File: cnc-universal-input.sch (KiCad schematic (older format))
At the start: 161 parts, among them J1 SA, J10 pwr-in, J11 output, J12 USB_B_Mini, J13 ext-pwr, J2 SB, J3 SC, J4 SD, J5 SE, J6 SF, J7 SG, J8 SH, J9 AVR-ISP-6, Q1 2N7002, Q10 IRLML2244TRPBF, Q11 2N7002, Q12 2N7002, Q13 2N7002, Q2 2N7002, Q3 2N7002, Q4 2N7002, Q5 2N7002, Q6 2N7002, Q7 2N7002, Q8 2N7002, Q9 2N7002, SW1 RESET, SW2 BTN, U1 ATmega328PB, U10 SFH617A-4, U11 SFH617A-4, U12 SFH617A-4, U13 SFH617A-4, U14 SFH617A-4, U15 SFH617A-4, U16 SFH617A-4, U17 SFH617A-4, U18 CH340G, U2 74HC595, U3 74HC595, U4 74HC595, U5 4051, U6 L7812, U7 L7805, U8 LM7321, U9 SFH617A-4, Y1 20Mhz, Y2 12MHz

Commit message: Fixed 340G isolation issue
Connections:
- net labels removed: VBUS
- wire segments 586 -> 580
- no-connect marks 12 -> 13
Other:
- moved on the sheet: C10, C21
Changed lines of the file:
@@
 Wire Wire Line
 	14600 6050 14600 6100
-$Comp
-L power:VBUS #PWR0175
-U 1 1 600B49CF
-P 14600 4500
-F 0 "#PWR0175" H 14600 4350 50  0001 C CNN
-F 1 "VBUS" H 14615 4673 50  0000 C CNN
-F 2 "" H 14600 4500 50  0001 C CNN
-F 3 "" H 14600 4500 50  0001 C CNN
-	1    14600 4500
-	1    0    0    -1
-$EndComp
 Wire Wire Line
 	14600 4500 14600 4850
@@
 	15400 4550 15400 4500
 $Comp
-L power:VBUS #PWR0177
-U 1 1 609D5862
-P 15150 4500
-F 0 "#PWR0177" H 15150 4350 50  0001 C CNN
-F 1 "VBUS" H 15165 4673 50  0000 C CNN
-F 2 "" H 15150 4500 50  0001 C CNN
-F 3 "" H 15150 4500 50  0001 C CNN
-	1    15150 4500
-	1    0    0    -1
-$EndComp
-$Comp
-L power:VBUS #PWR0178
-U 1 1 609D5BF4
-P 15400 4500
-F 0 "#PWR0178" H 15400 4350 50  0001 C CNN
-F 1 "VBUS" H 15415 4673 50  0000 C CNN
-F 2 "" H 15400 4500 50  0001 C CNN
-F 3 "" H 15400 4500 50  0001 C CNN
-	1    15400 4500
-	1    0    0    -1
-$EndComp
-$Comp
 L cnc-universal-input-rescue:USB_B_Mini-Connector J12
 U 1 1 609D7711
@@
 NoConn ~ 13450 5550
 $Comp
-L power:VBUS #PWR0179
-U 1 1 60ABEF15
-P 13500 4500
-F 0 "#PWR0179" H 13500 4350 50  0001 C CNN
-F 1 "VBUS" H 13515 4673 50  0000 C CNN
-F 2 "" H 13500 4500 50  0001 C CNN
-F 3 "" H 13500 4500 50  0001 C CNN
-	1    13500 4500
-	1    0    0    -1
-$EndComp
-Wire Wire Line
-	13500 4500 13500 4750
-Wire Wire Line
-	13500 5150 13450 5150
-$Comp
 L power:GND #PWR0180
 U 1 1 60B0DB32
@@
 L Device:CP_Small C10
 U 1 1 6112AB08
-P 13750 4900
-F 0 "C10" V 13838 4946 50  0000 L CNN
-F 1 "10uF" V 13600 4750 50  0000 L CNN
-F 2 "Capacitor_Tantalum_SMD:CP_EIA-6032-28_Kemet-C" H 13750 4900 50  0001 C CNN
-F 3 "~" H 13750 4900 50  0001 C CNN
-	1    13750 4900
-	1    0    0    -1
-$EndComp
-Wire Wire Line
-	13750 4800 13750 4750
-Wire Wire Line
-	13750 4750 13500 4750
-Connection ~ 13500 4750
-Wire Wire Line
-	13500 4750 13500 5150
+P 15300 5950
+F 0 "C10" V 15388 5996 50  0000 L CNN
+F 1 "10uF" V 15150 5800 50  0000 L CNN
+F 2 "Capacitor_Tantalum_SMD:CP_EIA-6032-28_Kemet-C" H 15300 5950 50  0001 C CNN
+F 3 "~" H 15300 5950 50  0001 C CNN
+	1    15300 5950
+	1    0    0    -1
+$EndComp
 $Comp
 L power:GND #PWR0181
 U 1 1 6117C62D
-P 13750 5050
-F 0 "#PWR0181" H 13750 4800 50  0001 C CNN
-F 1 "GND" H 13755 4877 50  0000 C CNN
-F 2 "" H 13750 5050 50  0001 C CNN
-F 3 "" H 13750 5050 50  0001 C CNN
-	1    13750 5050
-	1    0    0    -1
-$EndComp
-Wire Wire Line
-	13750 5000 13750 5050
+P 15300 6050
+F 0 "#PWR0181" H 15300 5800 50  0001 C CNN
+F 1 "GND" H 15305 5877 50  0000 C CNN
+F 2 "" H 15300 6050 50  0001 C CNN
+F 3 "" H 15300 6050 50  0001 C CNN
+	1    15300 6050
+	1    0    0    -1
+$EndComp
 Wire Notes Line
 	15800 4200 15800 6400
@@
 L Device:C_Small C21
 U 1 1 605F6BC3
-P 15350 6000
-F 0 "C21" H 15442 6046 50  0000 L CNN
-F 1 "100nF" V 15550 5750 50  0000 L CNN
-F 2 "Capacitor_SMD:C_0805_2012Metric" H 15350 6000 50  0001 C CNN
-F 3 "~" H 15350 6000 50  0001 C CNN
-	1    15350 6000
+P 15550 5950
+F 0 "C21" H 15642 5996 50  0000 L CNN
+F 1 "100nF" V 15750 5700 50  0000 L CNN
+F 2 "Capacitor_SMD:C_0805_2012Metric" H 15550 5950 50  0001 C CNN
+F 3 "~" H 15550 5950 50  0001 C CNN
+	1    15550 5950
 	1    0    0    -1
 $EndComp
@@
 L power:GND #PWR0198
 U 1 1 605F6BCF
-P 15350 6100
-F 0 "#PWR0198" H 15350 5850 50  0001 C CNN
-F 1 "GND" H 15350 5950 50  0000 C CNN
-F 2 "" H 15350 6100 50  0001 C CNN
-F 3 "" H 15350 6100 50  0001 C CNN
-	1    15350 6100
-	1    0    0    -1
-$EndComp
-$Comp
-L power:VBUS #PWR0199
-U 1 1 6064EB08
-P 15350 5900
-F 0 "#PWR0199" H 15350 5750 50  0001 C CNN
-F 1 "VBUS" H 15365 6073 50  0000 C CNN
-F 2 "" H 15350 5900 50  0001 C CNN
-F 3 "" H 15350 5900 50  0001 C CNN
-	1    15350 5900
+P 15550 6050
+F 0 "#PWR0198" H 15550 5800 50  0001 C CNN
+F 1 "GND" H 15550 5900 50  0000 C CNN
+F 2 "" H 15550 6050 50  0001 C CNN
+F 3 "" H 15550 6050 50  0001 C CNN
+	1    15550 6050
 	1    0    0    -1
 $EndComp
@@
 	1    0    0    -1
 $EndComp
+NoConn ~ 13450 5150
+$Comp
+L power:+5V #PWR0175
+U 1 1 6034F777
+P 14600 4500
+F 0 "#PWR0175" H 14600 4350 50  0001 C CNN
+F 1 "+5V" H 14615 4673 50  0000 C CNN
+F 2 "" H 14600 4500 50  0001 C CNN
+F 3 "" H 14600 4500 50  0001 C CNN
+	1    14600 4500
+	1    0    0    -1
+$EndComp
+$Comp
+L power:+5V #PWR0177
+U 1 1 60350634
+P 15150 4500
+F 0 "#PWR0177" H 15150 4350 50  0001 C CNN
+F 1 "+5V" H 15165 4673 50  0000 C CNN
+F 2 "" H 15150 4500 50  0001 C CNN
+F 3 "" H 15150 4500 50  0001 C CNN
+	1    15150 4500
+	1    0    0    -1
+$EndComp
+$Comp
+L power:+5V #PWR0179
+U 1 1 60469C21
+P 15550 5850
+F 0 "#PWR0179" H 15550 5700 50  0001 C CNN
+F 1 "+5V" H 15565 6023 50  0000 C CNN
+F 2 "" H 15550 5850 50  0001 C CNN
+F 3 "" H 15550 5850 50  0001 C CNN
+	1    15550 5850
+	1    0    0    -1
+$EndComp
+$Comp
+L power:+5V #PWR0199
+U 1 1 604C7554
+P 15300 5850
+F 0 "#PWR0199" H 15300 5700 50  0001 C CNN
+F 1 "+5V" H 15315 6023 50  0000 C CNN
+F 2 "" H 15300 5850 50  0001 C CNN
+F 3 "" H 15300 5850 50  0001 C CNN
+	1    15300 5850
+	1    0    0    -1
+$EndComp
+$Comp
+L power:+5V #PWR?
+U 1 1 604EB703
+P 15400 4500
+F 0 "#PWR?" H 15400 4350 50  0001 C CNN
+F 1 "+5V" H 15415 4673 50  0000 C CNN
+F 2 "" H 15400 4500 50  0001 C CNN
+F 3 "" H 15400 4500 50  0001 C CNN
+	1    15400 4500
+	1    0    0    -1
+$EndComp

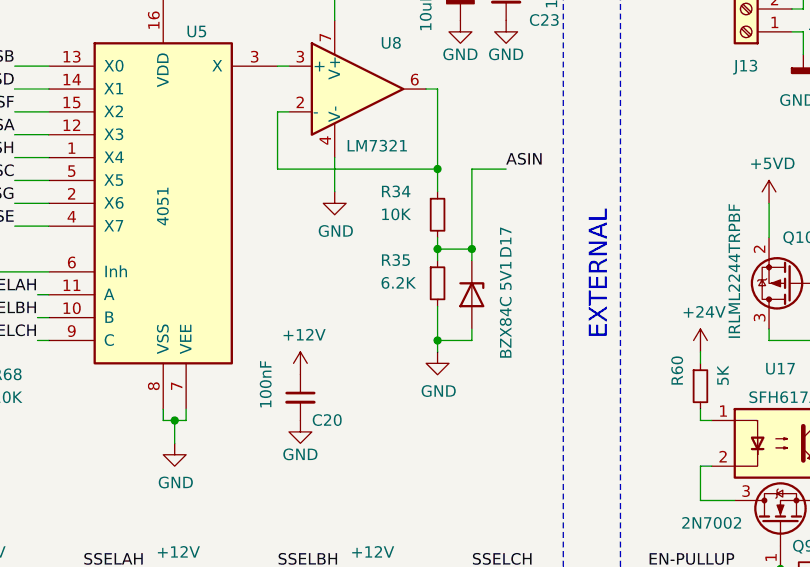
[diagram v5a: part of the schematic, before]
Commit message: Changed the voltage divider
Forgot to change R2 to 10K/7K so the input voltage to the adc was a bit low. 4.5 instead of 4.9.
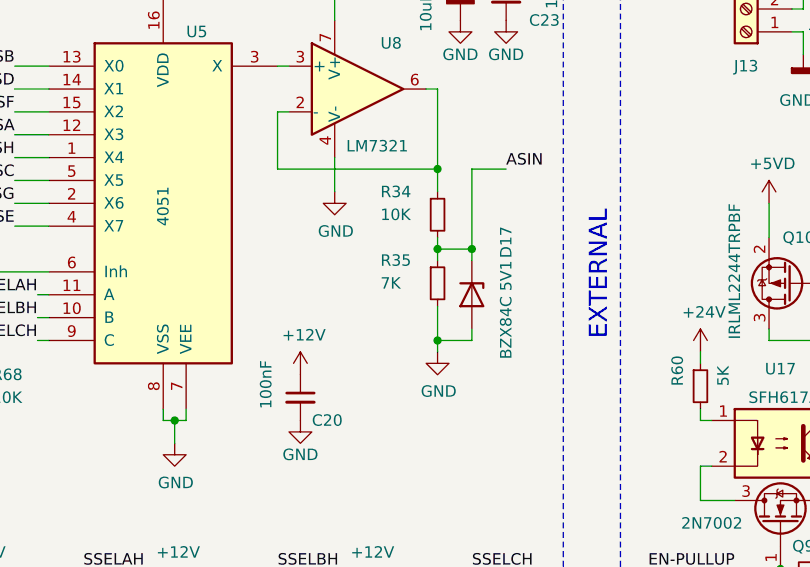
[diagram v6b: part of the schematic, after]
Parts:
- R35: value 6.2K -> 7K
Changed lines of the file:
@@
 P 13550 2150
 F 0 "R35" H 13300 2250 50  0000 L CNN
-F 1 "6.2K" H 13300 2150 50  0000 L CNN
+F 1 "7K" H 13300 2150 50  0000 L CNN
 F 2 "Resistor_SMD:R_0805_2012Metric" H 13550 2150 50  0001 C CNN
 F 3 "~" H 13550 2150 50  0001 C CNN

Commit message: Cleanup
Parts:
- removed C14, C8: 10uF, Capacitor_Tantalum_SMD:CP_EIA-6032-28_Kemet-C, symbol Device:CP_Small
- removed C5, C6: 100nF, Capacitor_SMD:C_0805_2012Metric, symbol Device:C_Small
- removed Q10: IRLML2244TRPBF, Package_TO_SOT_SMD:SOT-23, symbol Transistor_FET:IRLML5203
- removed Q2, Q3, Q4, Q5, Q6, Q7, Q8, Q9: 2N7002, Package_TO_SOT_SMD:SOT-23, symbol Transistor_FET:2N7002
- removed R10, R11, R12, R13, R14, R15, R16, R2, R3, R4, R44, R45, R46, R47, R5, R56, R57, R58, R59, R6, R7, R8, R9: 5K, Resistor_SMD:R_0805_2012Metric, symbol Device:R_Small
- removed R18, R19, R20, R21, R22, R23, R24, R25, R26, R27, R28, R29, R30, R31, R32, R33: 470, Resistor_SMD:R_0805_2012Metric, symbol Device:R_Small
- removed R36, R37, R38, R39, R48, R49, R50, R51: 2K, Resistor_SMD:R_0805_2012Metric, symbol Device:R_Small
- removed R40, R41, R42, R43, R52, R53, R54, R55, R61, R62, R63: 10K, Resistor_SMD:R_0805_2012Metric, symbol Device:R_Small
- removed U17: SFH617A-4, Package_DIP:DIP-4_W7.62mm_Socket, symbol Isolator:SFH617A-4
- removed U6: L7812, Package_TO_SOT_SMD:TO-263-2, symbol Regulator_Linear:L7812
- removed U7: L7805, Package_TO_SOT_SMD:TO-263-2, symbol Regulator_Linear:L7805
- added BZ1: Buzzer, Buzzer_Beeper:Buzzer_TDK_PS1240P02BT_D12.2mm_H6.5mm, symbol Device:Buzzer
- added C14, C26, C8: 100nF, Capacitor_SMD:C_0805_2012Metric, symbol Device:C_Small
- added C24: 10nF, Capacitor_SMD:C_0805_2012Metric, symbol Device:C_Small
- added C25, C27, C28, C5: 10uF, Capacitor_SMD:CP_Elec_4x5.4, symbol Device:CP_Small
- added C6: 220uF, Capacitor_SMD:CP_Elec_6.3x7.7, symbol Device:CP_Small
- added D20, D21: B240F, Diode_SMD:D_2114_3652Metric, symbol Device:D_Schottky_Small
- added D22: LEDB, Diode_SMD:D_0805_2012Metric, symbol Device:LED_Small
- added D23, D24, D25, D26: BAT54A, Package_TO_SOT_SMD:SOT-23, symbol Diode:BAT54A
- added J14: 2PT, TerminalBlock_RND:TerminalBlock_RND_205-00001_1x02_P5.00mm_Horizontal, symbol Connector:Screw_Terminal_01x02
- added L1, L2: 68uH, Inductor_SMD:L_6.3x6.3_H3, symbol Device:L_Small
- added R72: 4.7K, Resistor_SMD:R_0805_2012Metric, symbol Device:R_Small
- added R73: 1.5K, Resistor_SMD:R_0805_2012Metric, symbol Device:R_Small
- added R74: 9.1K, Resistor_SMD:R_0805_2012Metric, symbol Device:R_Small
- added R75: 1K, Resistor_SMD:R_0805_2012Metric, symbol Device:R_Small
- added RN1, RN2: 10KP4, Resistor_SMD:R_Array_Convex_4x1206, symbol Device:R_Pack04
- added RN10, RN7, RN8, RN9: 4.7KP4, Resistor_SMD:R_Array_Convex_4x1206, symbol Device:R_Pack04
- added RN11, RN12, RN3, RN4, RN5, RN6: 470P4, Resistor_SMD:R_Array_Convex_4x1206, symbol Device:R_Pack04
- added U19, U6: TS2596S, Package_SO:SOP-8_3.9x4.9mm_P1.27mm, symbol IvyBit:TS2596S
- C1, C11, C12, C2: value 22pF -> 30pF
- C10, C22: footprint Capacitor_Tantalum_SMD:CP_EIA-6032-28_Kemet-C -> Capacitor_SMD:CP_Elec_4x5.4
- C15: value 100nF -> 10nF
- C3: value 10uF -> 150uF; footprint Capacitor_Tantalum_SMD:CP_EIA-6032-28_Kemet-C -> Capacitor_SMD:CP_Elec_6.3x7.7
- C7: value 10uF -> 220uF; footprint Capacitor_Tantalum_SMD:CP_EIA-6032-28_Kemet-C -> Capacitor_SMD:CP_Elec_6.3x7.7
- D1: value OA -> LEDO; footprint Diode_SMD:D_0805_2012Metric_Pad1.15x1.40mm_HandSolder -> Diode_SMD:D_0805_2012Metric
- D10: value SB -> LEDB
- D11: value SC -> LEDB
- D12: value SD -> LEDB
- D13: value SE -> LEDB
- D14: value SF -> LEDB
- D15: value SG -> LEDB
- D16: value SH -> LEDB
- D18: value RX -> LEDB
- D19: value TX -> LEDO
- D2: value OB -> LEDO
- D3: value OC -> LEDO
- D4: value OD -> LEDO
- D5: value OE -> LEDO
- D6: value OF -> LEDO
- D7: value OG -> LEDO
- D8: value OH -> LEDO
- D9: value SA -> LEDB
- J1: value SA -> 3PT
- J10: value pwr-in -> 2PT
- J11: value output -> 8PT
- J13: value ext-pwr -> 2PT
- J2: value SB -> 3PT
- J3: value SC -> 3PT
- J4: value SD -> 3PT
- J5: value SE -> 3PT
- J6: value SF -> 3PT
- J7: value SG -> 3PT
- J8: value SH -> 3PT
- R1: value 5K -> 330
- R35: value 7K -> 6.8K
- R60: value 5K -> 1K
- R66, R67: value 3K -> 2K
- U10, U11, U12, U13, U14, U15, U16, U9: footprint Package_DIP:DIP-4_W7.62mm_Socket -> Package_DIP:DIP-4_W7.62mm
- Y1: value 20Mhz -> 18.432Mhz
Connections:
- net +12V: now also C14.1, C24.1, C27.1, C28.1, J14.1 (Pin_1), L2.2, R74.2, RN7.5 (R4.2), RN7.6 (R3.2), RN7.7 (R2.2), RN7.8 (R1.2), RN9.5 (R4.2), RN9.6 (R3.2), RN9.7 (R2.2), RN9.8 (R1.2); no longer C15.1
- net +24V: now also U19.1 (VCC), U6.1 (VCC); no longer R60.1
- net +5V: now also C15.1, C5.1, C6.1, C8.1, J14.2 (Pin_2), L1.2, R72.2
- net +5VD: now also C25.1, C26.1, D23.3, D24.3, D25.3, D26.3
- net ASIN: now also U1.22 (ADC7)
- net GND: now also U10.2, U11.2, U12.2, U13.2, U14.2, U15.2, U16.2, U3.13 (~OE), U9.2, C14.2, C25.2, C26.2, C27.2, C28.2, C5.2, C6.2, C8.2, D20.2 (A), D21.2 (A), D22.1 (K), R73.1, R75.1, RN10.1 (R1.1), RN10.2 (R2.1), RN10.3 (R3.1), RN10.4 (R4.1), RN8.1 (R1.1), RN8.2 (R2.1), RN8.3 (R3.1), RN8.4 (R4.1), U19.4 (EN), U19.5 (VSS), U19.6 (VSS), U19.7 (VSS), U19.8 (VSS), U6.4 (EN), U6.5 (VSS), U6.6 (VSS), U6.7 (VSS), U6.8 (VSS); no longer C15.2
- net OUT-A: now also RN11.4 (R4.1); no longer Q1.1 (G)
- net OUT-B: now also RN11.3 (R3.1)
- net OUT-C: now also RN11.2 (R2.1)
- net OUT-D: now also RN11.1 (R1.1)
- net OUT-E: now also RN12.4 (R4.1)
- net OUT-F: now also RN12.3 (R3.1)
- net OUT-G: now also RN12.2 (R2.1)
- net OUT-H: now also RN12.1 (R1.1)
- net OUT-RCLK: now also U1.1 (PD3); no longer U1.2 (PD4), U2.12 (RCLK)
- net OUT-SER: no longer U2.14 (SER)
- net OUT-SRCLK: now also U1.2 (PD4); no longer U1.9 (PD5), U2.11 (SRCLK)
- net SA: now also RN7.4 (R4.1), RN8.5 (R4.2); no longer R1.2
- net SB: now also RN7.3 (R3.1), RN8.6 (R3.2)
- net SC: now also RN7.2 (R2.1), RN8.7 (R2.2)
- net SD: now also RN7.1 (R1.1), RN8.8 (R1.2)
- net SE: now also RN10.5 (R4.2), RN9.4 (R4.1)
- net SF: now also RN10.6 (R3.2), RN9.3 (R3.1)
- net SG: now also RN10.7 (R2.2), RN9.2 (R2.1)
- net SH: now also RN10.8 (R1.2), RN9.1 (R1.1)
- net ~OUT-SRCLR: now also U1.9 (PD5); no longer U1.10 (PD6), U2.10 (~SRCLR)
- net at D9.2 (A): now also RN3.4 (R4.1)
- net at U4.15 (QA): now also RN3.5 (R4.2)
- net at U4.1 (QB): now also RN3.6 (R3.2)
- net at U4.2 (QC): now also RN3.7 (R2.2)
- net at U4.3 (QD): now also RN3.8 (R1.2)
- net at U4.4 (QE): now also RN4.5 (R4.2)
- net at U4.5 (QF): now also RN4.6 (R3.2)
- net at U4.6 (QG): now also RN4.7 (R2.2)
- net at U4.7 (QH): now also RN4.8 (R1.2)
- net DISP-SER2: now reaches U4.9 (QH')
- net DISP-SER2: now also U2.14 (SER)
- net at D10.2 (A): now also RN3.3 (R3.1)
- net at D11.2 (A): now also RN3.2 (R2.1)
- net at D12.2 (A): now also RN3.1 (R1.1)
- net at D13.2 (A): now also RN4.4 (R4.1)
- net at D14.2 (A): now also RN4.3 (R3.1)
- net at D15.2 (A): now also RN4.2 (R2.1)
- net at D16.2 (A): now also RN4.1 (R1.1)
- net at D1.2 (A): now also RN5.4 (R4.1)
- net at U2.15 (QA): now also RN5.5 (R4.2)
- net at U2.1 (QB): now also RN5.6 (R3.2)
- net at U2.2 (QC): now also RN5.7 (R2.2)
- net at U2.3 (QD): now also RN5.8 (R1.2)
- net at U2.4 (QE): now also RN6.5 (R4.2)
- net at U2.5 (QF): now also RN6.6 (R3.2)
- net at U2.6 (QG): now also RN6.7 (R2.2)
- net at U2.7 (QH): now also RN6.8 (R1.2)
- net at D2.2 (A): now also RN5.3 (R3.1)
- net at D3.2 (A): now also RN5.2 (R2.1)
- net at D4.2 (A): now also RN5.1 (R1.1)
- net at D5.2 (A): now also RN6.4 (R4.1)
- net at D6.2 (A): now also RN6.3 (R3.1)
- net at D7.2 (A): now also RN6.2 (R2.1)
- net at D8.2 (A): now also RN6.1 (R1.1)
- net at Q1.3 (D): now also BZ1.2 (+); no longer U9.2
- net POA: now reaches U9.1
- net POA: now also RN11.5 (R4.2)
- net at R60.2: now also D22.2 (A)
- net POB: now reaches U10.1
- net POB: now also RN11.6 (R3.2)
- net POC: now reaches U11.1
- net POC: now also RN11.7 (R2.2)
- net POD: now reaches U12.1
- net POD: now also RN11.8 (R1.2)
- net POE: now reaches U13.1
- net POE: now also RN12.5 (R4.2)
- net POF: now reaches U14.1
- net POF: now also RN12.6 (R3.2)
- net POG: now reaches U15.1
- net POG: now also RN12.7 (R2.2)
- net POH: now reaches U16.1
- net POH: now also RN12.8 (R1.2)
- net EN-PULLUP: no longer names the net of U1.11 (PD7)
- net EN-PULLUP: now also R60.1
- net IN-RCLK renamed DISP-RCLK
- net DISP-RCLK: now also U2.12 (RCLK)
- net IN-SER renamed DISP-SER
- net IN-SRCLK renamed DISP-SRCLK
- net DISP-SRCLK: now also U2.11 (SRCLK)
- net OA renamed BA
- net BA: now also RN1.1 (R1.1)
- net OB renamed BB
- net BB: now also RN1.2 (R2.1)
- net OC renamed BC
- net BC: now also RN1.3 (R3.1)
- net OD renamed BD
- net BD: now also RN1.4 (R4.1)
- net OE renamed BE
- net BE: now also RN2.1 (R1.1)
- net OF renamed BF
- net BF: now also RN2.2 (R2.1)
- net OG renamed BG
- net BG: now also RN2.3 (R3.1)
- net OH renamed BH
- net BH: now also RN2.4 (R4.1)
- net ~IN-OE renamed ~DISP-OE
- net ~DISP-OE: now also U2.13 (~OE)
- net ~IN-SRCLR renamed ~DISP-SRCLR
- net ~DISP-SRCLR: now also U2.10 (~SRCLR)
- removed net ~OUT-OE: U1.1 (PD3), U2.13 (~OE), U3.13 (~OE)
- new net: D20.1 (K), L1.1, U19.2 (SW)
- new net: C15.2, R72.1, R73.2, U19.3 (FB)
- new net: D23.1, RN1.8 (R1.2)
- new net: D23.2, RN1.7 (R2.2)
- new net: D24.1, RN1.6 (R3.2)
- new net: D24.2, RN1.5 (R4.2)
- new net: D21.1 (K), L2.1, U6.2 (SW)
- new net: C24.2, R74.1, R75.2, U6.3 (FB)
- new net: D25.2, RN2.5 (R4.2)
- new net: D25.1, RN2.6 (R3.2)
- new net: D26.2, RN2.7 (R2.2)
- new net: D26.1, RN2.8 (R1.2)
- new net: BZ1.1 (-), R1.2
- new net TO: Q1.1 (G), U1.10 (PD6)
- no-connect marks 13 -> 12
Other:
- moved on the sheet: C17, C18, C19, C20, C22, C23, J10, J11, J13, J9, Q11, Q12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

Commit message: crap!
wrong foot print
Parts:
- RN1, RN10, RN11, RN12, RN2, RN3, RN4, RN5, RN6, RN7, RN8, RN9: footprint Resistor_SMD:R_Array_Convex_4x1206 -> Resistor_SMD:R_Array_Convex_4x0603
- U19, U6: symbol IvyBit:TS2596S -> cnc-universal-input-rescue:TS2596S-IvyBit
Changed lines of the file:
@@
 ~DISP-OE
 $Comp
-L IvyBit:TS2596S U19
+L cnc-universal-input-rescue:TS2596S-IvyBit U19
 U 1 1 608DC45B
 P 3550 6100
@@
 Connection ~ 5650 5700
 $Comp
-L IvyBit:TS2596S U6
+L cnc-universal-input-rescue:TS2596S-IvyBit U6
 U 1 1 61622B4D
 P 3550 7550
@@
 F 0 "RN1" V 15775 2000 50  0000 C CNN
 F 1 "10KP4" V 15684 2000 50  0000 C CNN
-F 2 "Resistor_SMD:R_Array_Convex_4x1206" V 15725 2000 50  0001 C CNN
+F 2 "Resistor_SMD:R_Array_Convex_4x0603" V 15725 2000 50  0001 C CNN
 F 3 "~" H 15450 2000 50  0001 C CNN
 	1    15450 2000
@@
 F 0 "RN2" V 15775 2950 50  0000 C CNN
 F 1 "10KP4" V 15684 2950 50  0000 C CNN
-F 2 "Resistor_SMD:R_Array_Convex_4x1206" V 15725 2950 50  0001 C CNN
+F 2 "Resistor_SMD:R_Array_Convex_4x0603" V 15725 2950 50  0001 C CNN
 F 3 "~" H 15450 2950 50  0001 C CNN
 	1    15450 2950
@@
 F 0 "RN3" V 8125 1200 50  0000 C CNN
 F 1 "470P4" V 8034 1200 50  0000 C CNN
-F 2 "Resistor_SMD:R_Array_Convex_4x1206" V 8075 1200 50  0001 C CNN
+F 2 "Resistor_SMD:R_Array_Convex_4x0603" V 8075 1200 50  0001 C CNN
 F 3 "~" H 7800 1200 50  0001 C CNN
 	1    7800 1200
@@
 F 0 "RN4" V 7350 1600 50  0000 C CNN
 F 1 "470P4" V 7450 1600 50  0000 C CNN
-F 2 "Resistor_SMD:R_Array_Convex_4x1206" V 8075 1600 50  0001 C CNN
+F 2 "Resistor_SMD:R_Array_Convex_4x0603" V 8075 1600 50  0001 C CNN
 F 3 "~" H 7800 1600 50  0001 C CNN
 	1    7800 1600
@@
 F 0 "RN5" V 5275 1200 50  0000 C CNN
 F 1 "470P4" V 5184 1200 50  0000 C CNN
-F 2 "Resistor_SMD:R_Array_Convex_4x1206" V 5225 1200 50  0001 C CNN
+F 2 "Resistor_SMD:R_Array_Convex_4x0603" V 5225 1200 50  0001 C CNN
 F 3 "~" H 4950 1200 50  0001 C CNN
 	1    4950 1200
@@
 F 0 "RN6" V 4500 1600 50  0000 C CNN
 F 1 "470P4" V 4600 1600 50  0000 C CNN
-F 2 "Resistor_SMD:R_Array_Convex_4x1206" V 5225 1600 50  0001 C CNN
+F 2 "Resistor_SMD:R_Array_Convex_4x0603" V 5225 1600 50  0001 C CNN
 F 3 "~" H 4950 1600 50  0001 C CNN
 	1    4950 1600
@@
 F 0 "RN7" V 10900 3050 50  0000 C CNN
 F 1 "4.7KP4" V 10800 3050 50  0000 C CNN
-F 2 "Resistor_SMD:R_Array_Convex_4x1206" V 10875 3050 50  0001 C CNN
+F 2 "Resistor_SMD:R_Array_Convex_4x0603" V 10875 3050 50  0001 C CNN
 F 3 "~" H 10600 3050 50  0001 C CNN
 	1    10600 3050
@@
 F 0 "RN8" V 12100 3050 50  0000 C CNN
 F 1 "4.7KP4" V 12000 3050 50  0000 C CNN
-F 2 "Resistor_SMD:R_Array_Convex_4x1206" V 12075 3050 50  0001 C CNN
+F 2 "Resistor_SMD:R_Array_Convex_4x0603" V 12075 3050 50  0001 C CNN
 F 3 "~" H 11800 3050 50  0001 C CNN
 	1    11800 3050
@@
 F 0 "RN9" V 10150 3450 50  0000 C CNN
 F 1 "4.7KP4" V 10250 3450 50  0000 C CNN
-F 2 "Resistor_SMD:R_Array_Convex_4x1206" V 10875 3450 50  0001 C CNN
+F 2 "Resistor_SMD:R_Array_Convex_4x0603" V 10875 3450 50  0001 C CNN
 F 3 "~" H 10600 3450 50  0001 C CNN
 	1    10600 3450
@@
 F 0 "RN10" V 11350 3450 50  0000 C CNN
 F 1 "4.7KP4" V 11450 3450 50  0000 C CNN
-F 2 "Resistor_SMD:R_Array_Convex_4x1206" V 12075 3450 50  0001 C CNN
+F 2 "Resistor_SMD:R_Array_Convex_4x0603" V 12075 3450 50  0001 C CNN
 F 3 "~" H 11800 3450 50  0001 C CNN
 	1    11800 3450
@@
 F 0 "RN11" V 5750 3550 50  0000 C CNN
 F 1 "470P4" V 5650 3550 50  0000 C CNN
-F 2 "Resistor_SMD:R_Array_Convex_4x1206" V 5725 3550 50  0001 C CNN
+F 2 "Resistor_SMD:R_Array_Convex_4x0603" V 5725 3550 50  0001 C CNN
 F 3 "~" H 5450 3550 50  0001 C CNN
 	1    5450 3550
@@
 F 0 "RN12" V 5050 3950 50  0000 C CNN
 F 1 "470P4" V 5150 3950 50  0000 C CNN
-F 2 "Resistor_SMD:R_Array_Convex_4x1206" V 5725 3950 50  0001 C CNN
+F 2 "Resistor_SMD:R_Array_Convex_4x0603" V 5725 3950 50  0001 C CNN
 F 3 "~" H 5450 3950 50  0001 C CNN
 	1    5450 3950
